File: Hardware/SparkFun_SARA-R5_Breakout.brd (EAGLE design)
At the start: 76.2 x 50.8 mm, 253 parts, among them IC1 SN74AVC4T774PW, IC2 SN74AVC4T774PW, J13 TP, J17 NANO_SIM, J19 NI, Q1 310mA/60V/1.6Ω, Q2 310mA/60V/1.6Ω, Q3 310mA/60V/1.6Ω, Q4 310mA/60V/1.6Ω, Q5 20V/0.2A/8MHz/1.2Ω/1Vth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

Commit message: Updates after concept review
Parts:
- removed U$42: (no value), output:#TXD2#0
- added U$75: (no value), output:LTE_GNSS_BREAKOUT_#_SARA#R510M8S0
- U$72: device output:U#BLOX_SARA#R510M8S_BREAKOUT0 -> output:#TXD2_I#0
- moved U$72 29.9 mm to (14.0, 16.6), turned to 270 degrees
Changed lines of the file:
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@@
 <element name="C1" library="SparkFun-Capacitors" package="0603" value="0.1uF" x="10.16" y="12.446" smashed="yes" rot="R180">
 <attribute name="NAME" x="10.16" y="11.684" size="0.6096" layer="25" font="vector" ratio="20" rot="R180" align="bottom-center"/>
-<attribute name="PROD_ID" value="CAP-00810" x="8.89" y="-5.334" size="1.778" layer="27" font="vector" ratio="15" rot="R180" display="off"/>
+<attribute name="PROD_ID" value="CAP-08604" x="8.89" y="-5.334" size="1.778" layer="27" font="vector" ratio="15" rot="R180" display="off"/>
 <attribute name="VALUE" x="10.16" y="13.208" size="0.6096" layer="27" font="vector" ratio="20" rot="R180" align="top-center"/>
 </element>
@@
 <element name="C4" library="SparkFun-Capacitors" package="0603" value="0.1uF" x="10.16" y="21.844" smashed="yes" rot="R180">
 <attribute name="NAME" x="10.16" y="21.082" size="0.6096" layer="25" font="vector" ratio="20" rot="R180" align="bottom-center"/>
-<attribute name="PROD_ID" value="CAP-00810" x="10.16" y="21.844" size="1.778" layer="27" font="vector" ratio="15" rot="R180" display="off"/>
+<attribute name="PROD_ID" value="CAP-08604" x="10.16" y="21.844" size="1.778" layer="27" font="vector" ratio="15" rot="R180" display="off"/>
 <attribute name="VALUE" x="10.16" y="22.606" size="0.6096" layer="27" font="vector" ratio="20" rot="R180" align="top-center"/>
 </element>
@@
 <element name="C20" library="SparkFun-Capacitors" package="0603" value="0.1uF" x="58.801" y="31.115" smashed="yes" rot="R180">
 <attribute name="NAME" x="58.801" y="30.353" size="0.6096" layer="25" font="vector" ratio="20" rot="R180" align="bottom-center"/>
-<attribute name="PROD_ID" value="CAP-00810" x="58.801" y="31.115" size="1.778" layer="27" ratio="15" rot="R180" display="off"/>
+<attribute name="PROD_ID" value="CAP-08604" x="58.801" y="31.115" size="1.778" layer="27" ratio="15" rot="R180" display="off"/>
 <attribute name="VALUE" x="58.801" y="31.877" size="0.6096" layer="27" font="vector" ratio="20" rot="R180" align="top-center"/>
 </element>
@@
 <element name="C22" library="SparkFun-Capacitors" package="0603" value="0.1uF" x="44.831" y="22.225" smashed="yes" rot="R270">
 <attribute name="NAME" x="45.593" y="22.225" size="0.6096" layer="25" font="vector" ratio="20" rot="R270" align="bottom-center"/>
-<attribute name="PROD_ID" value="CAP-00810" x="44.831" y="22.225" size="1.778" layer="27" ratio="15" rot="R270" display="off"/>
+<attribute name="PROD_ID" value="CAP-08604" x="44.831" y="22.225" size="1.778" layer="27" ratio="15" rot="R270" display="off"/>
 <attribute name="VALUE" x="44.069" y="22.225" size="0.6096" layer="27" font="vector" ratio="20" rot="R270" align="top-center"/>
 </element>
 <element name="C23" library="SparkFun-Capacitors" package="0603" value="0.1uF" x="28.321" y="19.304" smashed="yes" rot="R180">
 <attribute name="NAME" x="28.321" y="18.542" size="0.6096" layer="25" font="vector" ratio="20" rot="R180" align="bottom-center"/>
-<attribute name="PROD_ID" value="CAP-00810" x="28.321" y="19.304" size="1.778" layer="27" ratio="15" rot="R180" display="off"/>
+<attribute name="PROD_ID" value="CAP-08604" x="28.321" y="19.304" size="1.778" layer="27" ratio="15" rot="R180" display="off"/>
 <attribute name="VALUE" x="28.321" y="20.066" size="0.6096" layer="27" font="vector" ratio="20" rot="R180" align="top-center"/>
 </element>
@@
 <element name="C6" library="SparkFun-Capacitors" package="0603" value="0.1uF" x="30.48" y="13.208" smashed="yes" rot="R180">
 <attribute name="NAME" x="30.48" y="12.446" size="0.6096" layer="25" font="vector" ratio="20" rot="R180" align="bottom-center"/>
-<attribute name="PROD_ID" value="CAP-00810" x="30.48" y="13.208" size="1.778" layer="27" ratio="15" rot="R180" display="off"/>
+<attribute name="PROD_ID" value="CAP-08604" x="30.48" y="13.208" size="1.778" layer="27" ratio="15" rot="R180" display="off"/>
 <attribute name="VALUE" x="30.48" y="13.97" size="0.6096" layer="27" font="vector" ratio="20" rot="R180" align="top-center"/>
 </element>
 <element name="C25" library="SparkFun-Capacitors" package="0603" value="0.1uF" x="15.621" y="15.5575" smashed="yes" rot="R180">
 <attribute name="NAME" x="15.621" y="13.5255" size="0.6096" layer="25" font="vector" ratio="20" rot="R180" align="bottom-center"/>
-<attribute name="PROD_ID" value="CAP-00810" x="15.621" y="15.5575" size="1.778" layer="27" ratio="15" rot="R180" display="off"/>
+<attribute name="PROD_ID" value="CAP-08604" x="15.621" y="15.5575" size="1.778" layer="27" ratio="15" rot="R180" display="off"/>
 <attribute name="VALUE" x="15.621" y="16.3195" size="0.6096" layer="27" font="vector" ratio="20" rot="R180" align="top-center"/>
 </element>
@@
 <element name="U$40" library="output" package="#RTS_I#0" value="" x="35.56" y="18.415" smashed="yes" rot="MR270"/>
 <element name="U$41" library="output" package="#DTR_TXD2_I#0" value="" x="38.1" y="20.828" smashed="yes" rot="MR270"/>
-<element name="U$42" library="output" package="#TXD2#0" value="" x="13.97" y="16.256" smashed="yes" rot="MR270"/>
 <element name="U$43" library="output" package="#DCD_RXD2_O#0" value="" x="40.64" y="20.955" smashed="yes" rot="MR270"/>
 <element name="U$44" library="output" package="#RXD2_O#0" value="" x="16.51" y="16.891" smashed="yes" rot="MR270"/>
@@
 <element name="U$15" library="output" package="#SARA_INT#0" value="" x="6.096" y="22.86" smashed="yes" rot="MR0"/>
 <element name="U$71" library="output" package="#SARA_INT#0" value="" x="45.212" y="45.085" smashed="yes" rot="MR0"/>
-<element name="U$72" library="output" package="U#BLOX_SARA#R510M8S_BREAKOUT0" value="" x="38.1" y="34.29" smashed="yes" rot="MR0"/>
 <element name="U$73" library="output" package="LTE_CATEGORY_M10" value="" x="29.21" y="48.26" smashed="yes" rot="MR0"/>
 <element name="U$74" library="output" package="LTE_CATEGORY_NB20" value="" x="29.21" y="45.72" smashed="yes" rot="MR0"/>
 <element name="LOGO2" library="SparkFun-Aesthetics" package="OSHW-LOGO-MINI" value="OSHW-LOGOMINI" x="69.85" y="11.43" smashed="yes" rot="MR0"/>
+<element name="U$75" library="output" package="LTE_GNSS_BREAKOUT_#_SARA#R510M8S0" value="" x="38.1" y="34.29" smashed="yes" rot="MR0"/>
+<element name="U$72" library="output" package="#TXD2_I#0" value="" x="13.97" y="16.637" smashed="yes" rot="MR270"/>
 </elements>
 <signals>
@@
 </signals>
 <mfgpreviewcolors>
-<mfgpreviewcolor name="soldermaskcolor" color="0xC8008000"/>
+<mfgpreviewcolor name="soldermaskcolor" color="0xC8FF0000"/>
 <mfgpreviewcolor name="silkscreencolor" color="0xFFFEFEFE"/>
 <mfgpreviewcolor name="backgroundcolor" color="0xFF282828"/>

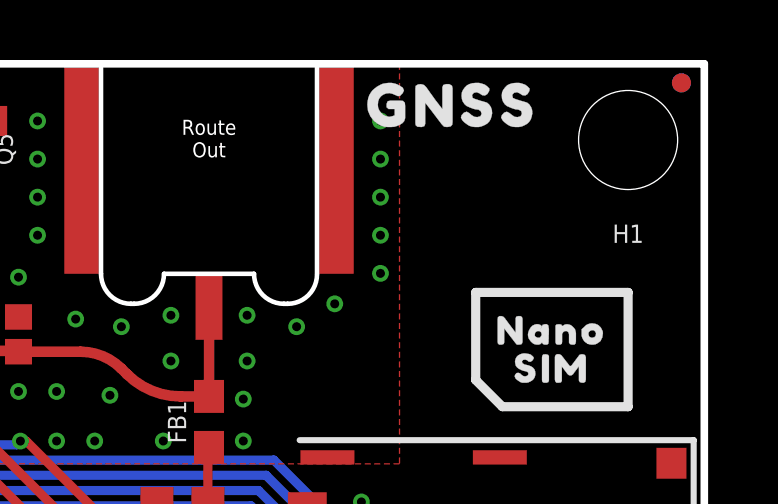
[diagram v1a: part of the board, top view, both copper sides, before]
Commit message: Update SparkFun_SARA-R5_Breakout.brd
Added L1 label to GNSS connector
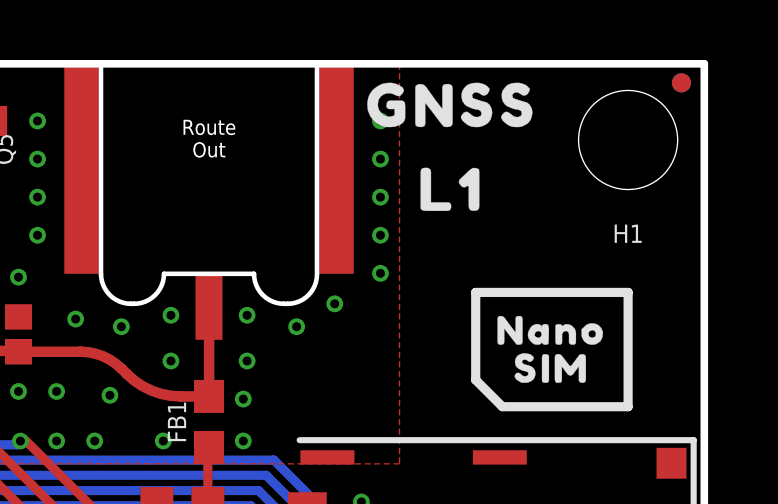
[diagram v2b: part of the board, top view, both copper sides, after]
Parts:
- added U$42: (no value), output:L10
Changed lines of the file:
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@@
 <layer number="17" name="Pads" color="2" fill="1" visible="yes" active="yes"/>
 <layer number="18" name="Vias" color="2" fill="1" visible="yes" active="yes"/>
-<layer number="19" name="Unrouted" color="13" fill="1" visible="yes" active="yes"/>
+<layer number="19" name="Unrouted" color="6" fill="1" visible="yes" active="yes"/>
 <layer number="20" name="Dimension" color="24" fill="1" visible="yes" active="yes"/>
 <layer number="21" name="tPlace" color="16" fill="1" visible="yes" active="yes"/>
@@
 <layer number="23" name="tOrigins" color="15" fill="1" visible="yes" active="yes"/>
 <layer number="24" name="bOrigins" color="15" fill="1" visible="yes" active="yes"/>
-<layer number="25" name="tNames" color="7" fill="1" visible="yes" active="yes"/>
-<layer number="26" name="bNames" color="7" fill="1" visible="yes" active="yes"/>
-<layer number="27" name="tValues" color="7" fill="1" visible="yes" active="yes"/>
-<layer number="28" name="bValues" color="7" fill="1" visible="yes" active="yes"/>
-<layer number="29" name="tStop" color="7" fill="3" visible="yes" active="yes"/>
-<layer number="30" name="bStop" color="7" fill="6" visible="yes" active="yes"/>
-<layer number="31" name="tCream" color="7" fill="4" visible="yes" active="yes"/>
-<layer number="32" name="bCream" color="7" fill="5" visible="yes" active="yes"/>
-<layer number="33" name="tFinish" color="6" fill="3" visible="yes" active="yes"/>
-<layer number="34" name="bFinish" color="6" fill="6" visible="yes" active="yes"/>
-<layer number="35" name="tGlue" color="7" fill="4" visible="yes" active="yes"/>
-<layer number="36" name="bGlue" color="7" fill="5" visible="yes" active="yes"/>
-<layer number="37" name="tTest" color="7" fill="1" visible="yes" active="yes"/>
-<layer number="38" name="bTest" color="7" fill="1" visible="yes" active="yes"/>
-<layer number="39" name="tKeepout" color="4" fill="11" visible="yes" active="yes"/>
-<layer number="40" name="bKeepout" color="1" fill="11" visible="yes" active="yes"/>
-<layer number="41" name="tRestrict" color="4" fill="10" visible="yes" active="yes"/>
-<layer number="42" name="bRestrict" color="1" fill="10" visible="yes" active="yes"/>
-<layer number="43" name="vRestrict" color="2" fill="10" visible="yes" active="yes"/>
-<layer number="44" name="Drills" color="7" fill="1" visible="yes" active="yes"/>
+<layer number="25" name="tNames" color="7" fill="1" visible="no" active="yes"/>
+<layer number="26" name="bNames" color="7" fill="1" visible="no" active="yes"/>
+<layer number="27" name="tValues" color="7" fill="1" visible="no" active="yes"/>
+<layer number="28" name="bValues" color="7" fill="1" visible="no" active="yes"/>
+<layer number="29" name="tStop" color="7" fill="3" visible="no" active="yes"/>
+<layer number="30" name="bStop" color="7" fill="6" visible="no" active="yes"/>
+<layer number="31" name="tCream" color="7" fill="4" visible="no" active="yes"/>
+<layer number="32" name="bCream" color="7" fill="5" visible="no" active="yes"/>
+<layer number="33" name="tFinish" color="6" fill="3" visible="no" active="yes"/>
+<layer number="34" name="bFinish" color="6" fill="6" visible="no" active="yes"/>
+<layer number="35" name="tGlue" color="7" fill="4" visible="no" active="yes"/>
+<layer number="36" name="bGlue" color="7" fill="5" visible="no" active="yes"/>
+<layer number="37" name="tTest" color="7" fill="1" visible="no" active="yes"/>
+<layer number="38" name="bTest" color="7" fill="1" visible="no" active="yes"/>
+<layer number="39" name="tKeepout" color="4" fill="11" visible="no" active="yes"/>
+<layer number="40" name="bKeepout" color="1" fill="11" visible="no" active="yes"/>
+<layer number="41" name="tRestrict" color="4" fill="10" visible="no" active="yes"/>
+<layer number="42" name="bRestrict" color="1" fill="10" visible="no" active="yes"/>
+<layer number="43" name="vRestrict" color="2" fill="10" visible="no" active="yes"/>
+<layer number="44" name="Drills" color="7" fill="1" visible="no" active="yes"/>
 <layer number="45" name="Holes" color="7" fill="1" visible="yes" active="yes"/>
-<layer number="46" name="Milling" color="3" fill="1" visible="yes" active="yes"/>
-<layer number="47" name="Measures" color="7" fill="1" visible="yes" active="yes"/>
-<layer number="48" name="Document" color="7" fill="1" visible="yes" active="yes"/>
-<layer number="49" name="Reference" color="7" fill="1" visible="yes" active="yes"/>
-<layer number="50" name="dxf" color="7" fill="1" visible="yes" active="yes"/>
+<layer number="46" name="Milling" color="3" fill="1" visible="no" active="yes"/>
+<layer number="47" name="Measures" color="7" fill="1" visible="no" active="yes"/>
+<layer number="48" name="Document" color="7" fill="1" visible="no" active="yes"/>
+<layer number="49" name="Reference" color="7" fill="1" visible="no" active="yes"/>
+<layer number="50" name="dxf" color="7" fill="1" visible="no" active="yes"/>
 <layer number="51" name="tDocu" color="6" fill="1" visible="yes" active="yes"/>
-<layer number="52" name="bDocu" color="7" fill="1" visible="yes" active="yes"/>
+<layer number="52" name="bDocu" color="7" fill="1" visible="no" active="yes"/>
 <layer number="91" name="Nets" color="2" fill="1" visible="no" active="no"/>
 <layer number="92" name="Busses" color="1" fill="1" visible="no" active="no"/>
@@
 <layer number="95" name="Names" color="7" fill="1" visible="no" active="no"/>
 <layer number="96" name="Values" color="7" fill="1" visible="no" active="no"/>
-<layer number="2" name="Route2" color="1" fill="3" visible="yes" active="yes"/>
-<layer number="15" name="Route15" color="4" fill="6" visible="yes" active="yes"/>
+<layer number="2" name="Route2" color="1" fill="3" visible="no" active="yes"/>
+<layer number="15" name="Route15" color="4" fill="6" visible="no" active="yes"/>
 <layer number="3" name="Route3" color="4" fill="3" visible="no" active="no"/>
 <layer number="4" name="Route4" color="1" fill="4" visible="no" active="no"/>
@@
 <element name="U$75" library="output" package="LTE_GNSS_BREAKOUT_#_SARA#R510M8S0" value="" x="38.1" y="34.29" smashed="yes" rot="MR0"/>
 <element name="U$72" library="output" package="#TXD2_I#0" value="" x="13.97" y="16.637" smashed="yes" rot="MR270"/>
+<element name="U$42" library="output" package="L10" value="" x="67.818" y="46.609" smashed="yes"/>
 </elements>
 <signals>

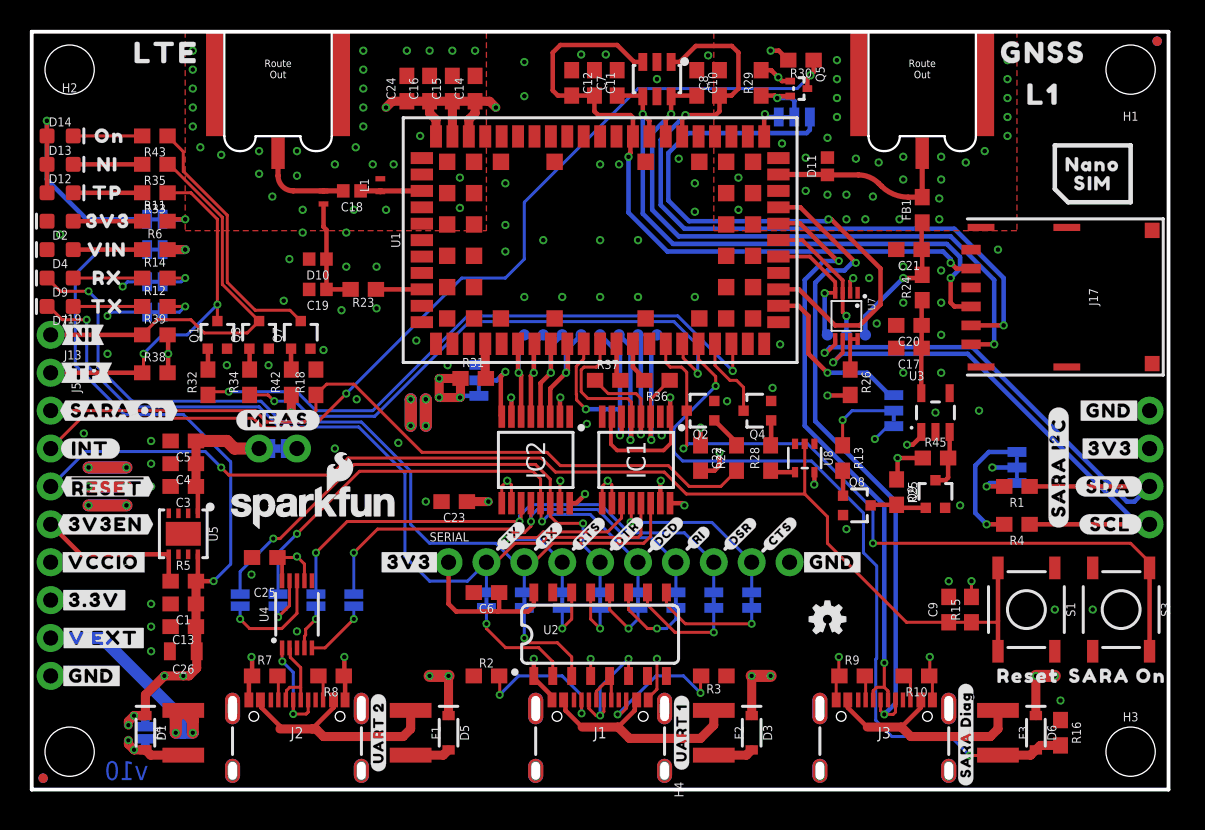
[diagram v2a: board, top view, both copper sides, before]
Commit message: Proto changes
Changed the version to v01
Changed led color of D7 from yellow to green
Switched text to vector
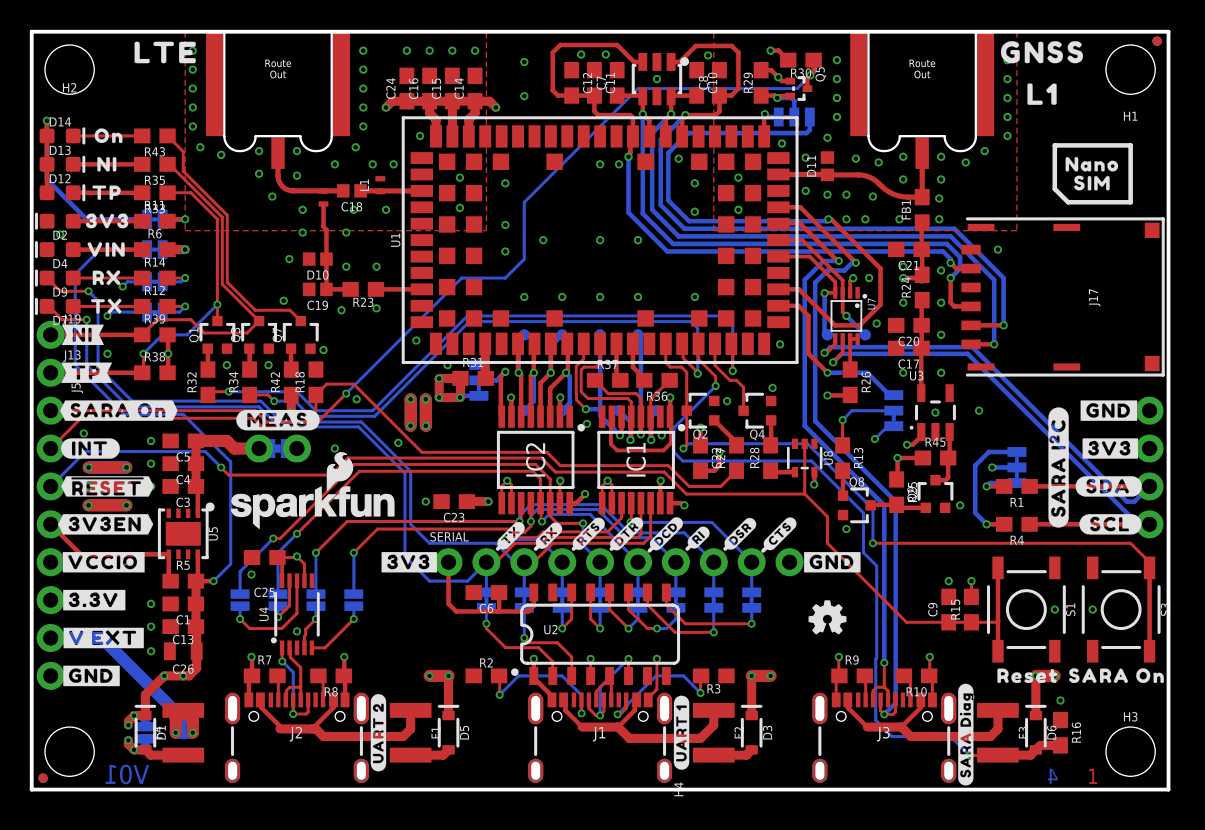
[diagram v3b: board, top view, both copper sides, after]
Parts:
- D7: value Yellow -> GREEN
- moved TP22 5.39 mm to (59.7, 34.3)
- moved TP14 5.24 mm to (35.6, 25.4)
- moved TP16 5.24 mm to (33.0, 25.4)
- moved TP1 5.08 mm to (41.9, 25.4)
- moved TP3 5.08 mm to (39.4, 25.4)
- moved TP10 1.27 mm to (55.9, 30.5)
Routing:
- net SARA_RXD_O: track 11.8 -> 6.67 mm
- net SARA_CTS_O: track 17.8 -> 12.7 mm
- net N$25: track 9.76 -> 6.17 mm
- net SARA_TP: track 41.8 -> 43.6 mm
- net SARA_RTS_I: track 15.7 -> 14.4 mm
- net SARA_NI: track 38.3 -> 38.9 mm
- net SARA_SCL_1.8V: track 9.18 -> 9.71 mm
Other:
- board text added: "1"
- board text added: "2"
- board text added: "3"
- board text added: "4"
- board text added: "V01"
- board text removed: "v10"
